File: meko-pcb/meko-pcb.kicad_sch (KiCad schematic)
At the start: 209 parts, among them IC2 TPS7A2033PDBVR, IC4 TAD5212IRGER, IC5 AS5600-ASOM, J1 USB_C_Receptacle_USB2.0_16P, J2 Conn_ARM_JTAG_SWD_10, J3 GDEY0154D67, J5 503398-1892, Q1 SS8050, Q2 Si1308EDL, SW1 SW_Push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

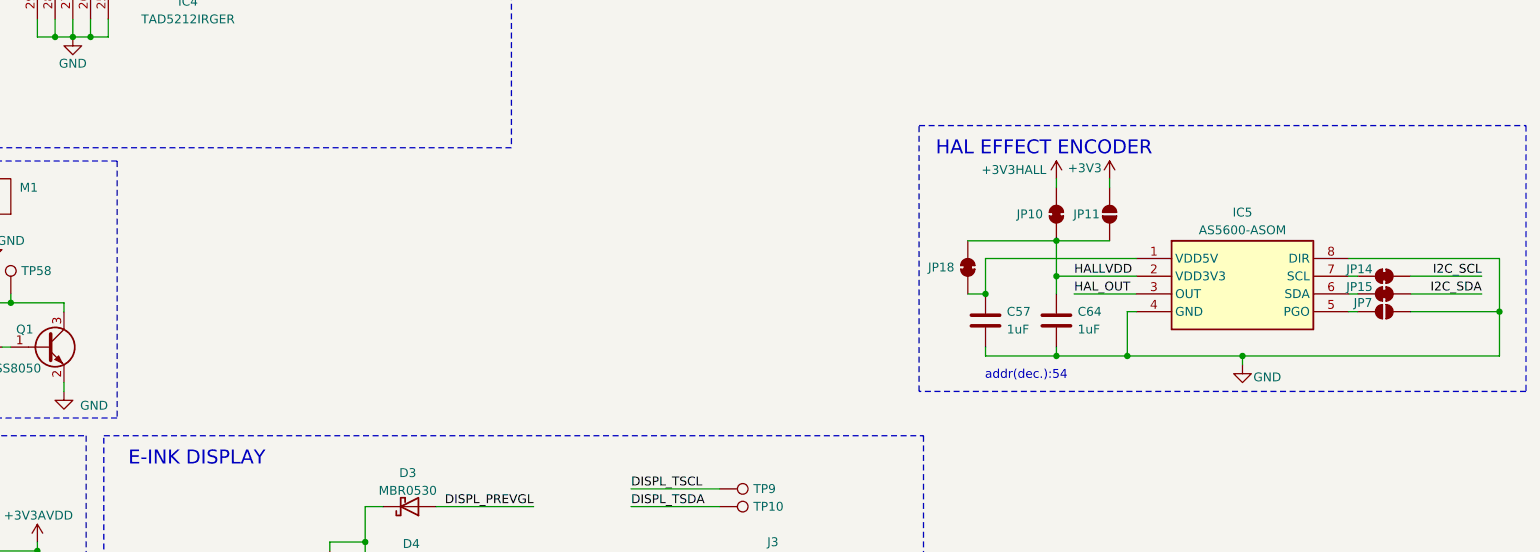
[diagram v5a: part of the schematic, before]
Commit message: updated a cap
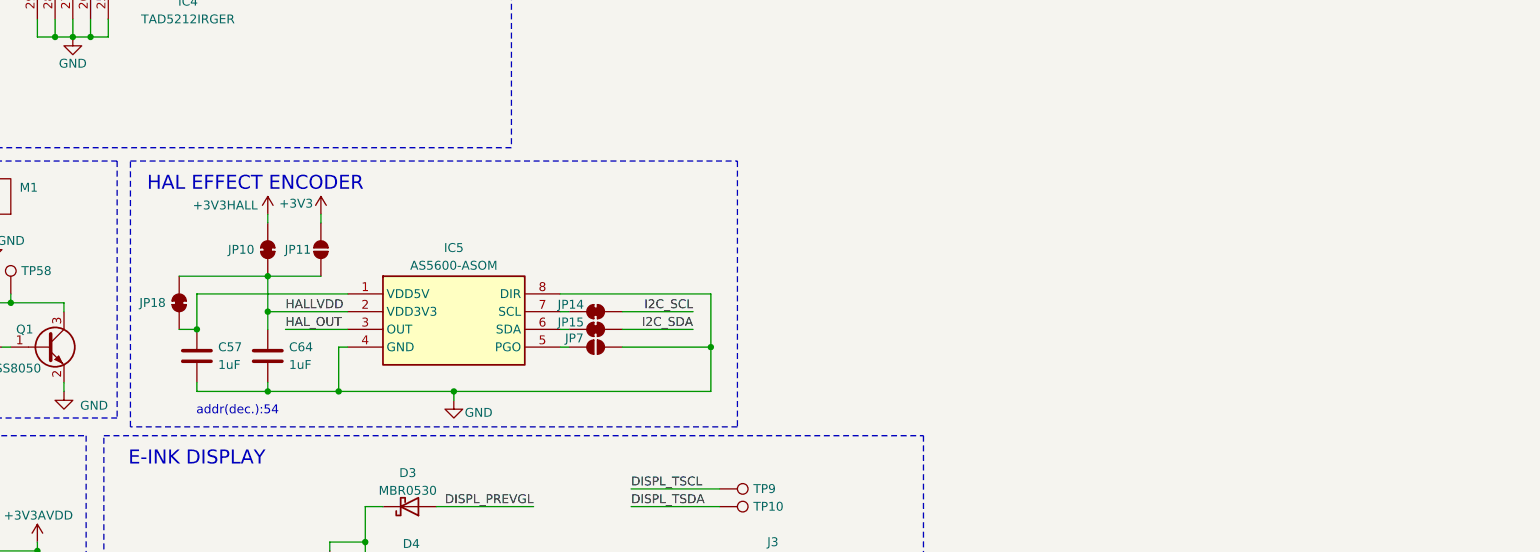
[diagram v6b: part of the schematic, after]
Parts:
- C18: LCSC C519367 -> C501844
- M1: LCSC (none) -> C2894731; LCSC Part Name LD-SM-430 -> (none); MPN LD-SM-430 -> (none); Manufacturer LEADER(立得) -> (none); Supplier LCSC -> (none); Supplier Part C41348533 -> (none)
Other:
- moved on the sheet: C57, C64, IC5, JP10, JP11, JP14, JP15, JP18, JP7

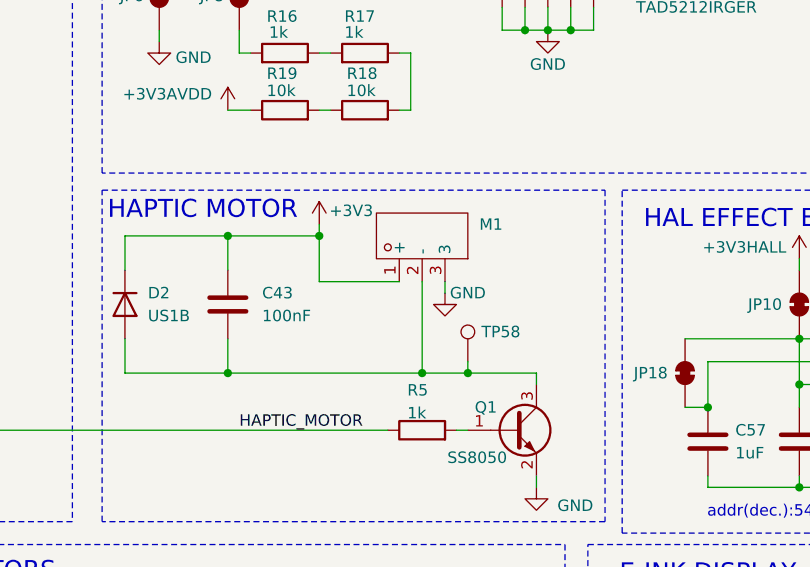
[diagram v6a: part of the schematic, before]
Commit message: updated motor foorprint, added 3d moedel
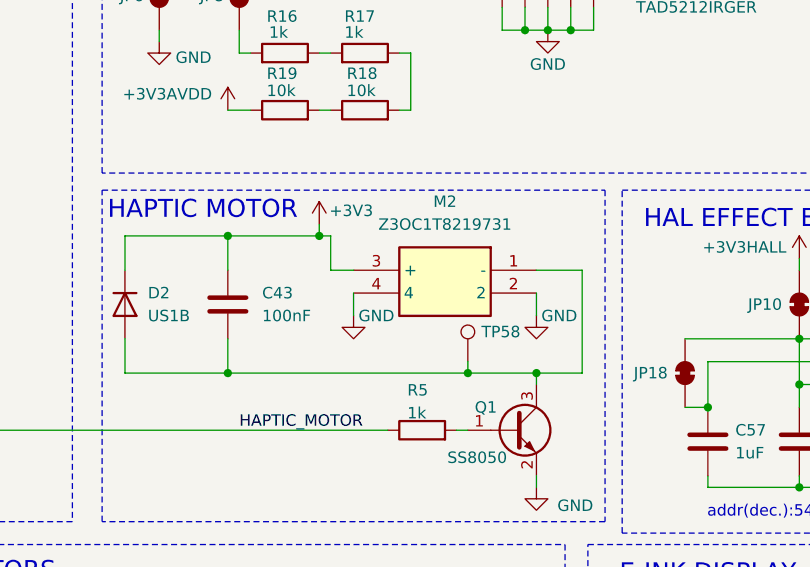
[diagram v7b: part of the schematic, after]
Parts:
- removed M1: ~, LD-SM-430:SMD_LD-SM-430-1, symbol LD-SM-430:LD-SM-430
- added M2: Z3OC1T8219731, Z3OC1T8219731:Z3OC1T8219731, symbol Z3OC1T8219731:Z3OC1T8219731
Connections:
- net +3V3: now also M2.3 (+)
- net GND: now also M2.2, M2.4
- net at C43.2, D2.2 (A), Q1.3 (C)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: now also M2.1 (-)

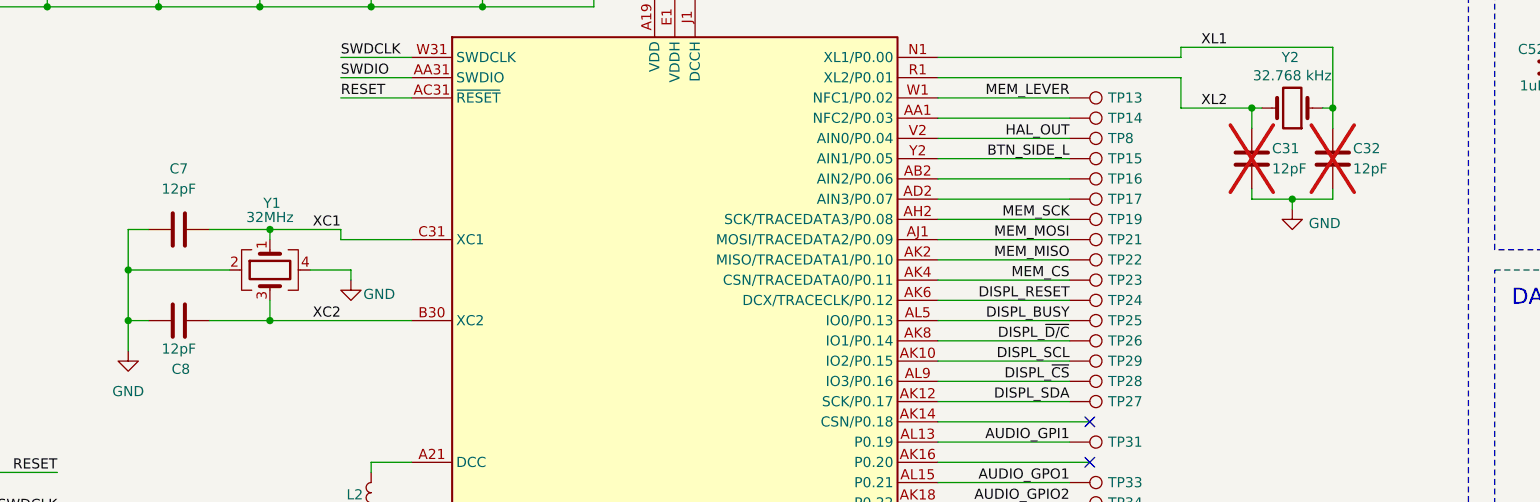
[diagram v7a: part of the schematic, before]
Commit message: chose a new crystal, so i can remove all 4 load caps
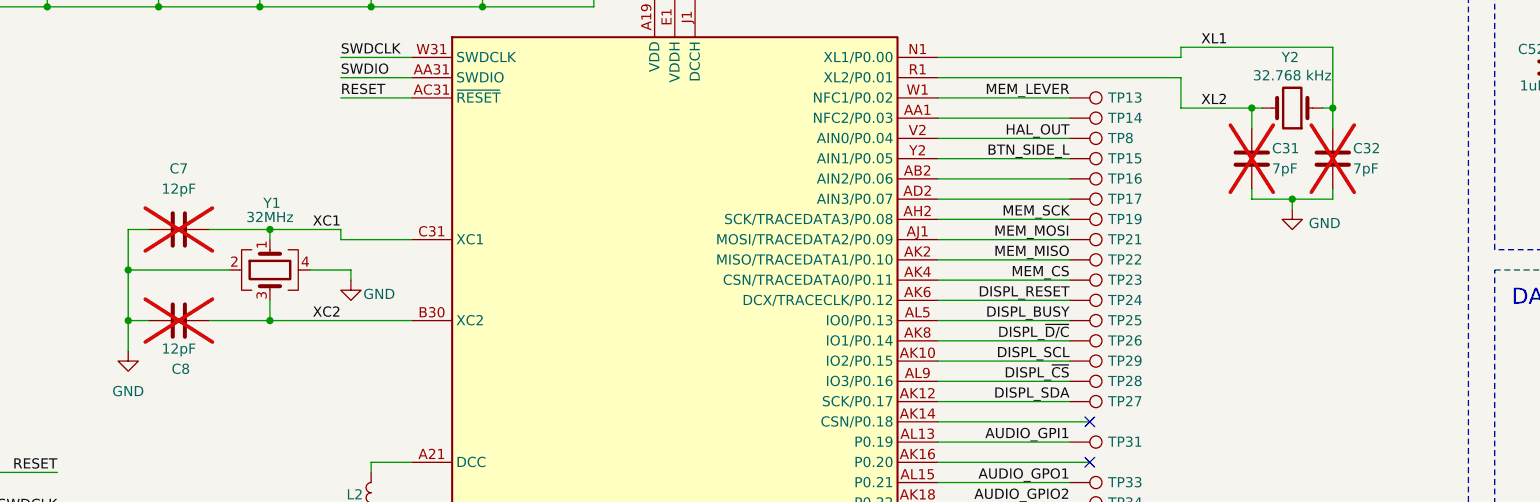
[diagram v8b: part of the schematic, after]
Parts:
- C31, C32: value 12pF -> 7pF; LCSC C38523 -> (none); MPN CL10C120JB8NNNC -> (none)
- C7, C8: now not fitted; now left out of the parts list
- Y2: LCSC C5213671 -> C90945
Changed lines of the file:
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@@
 			)
 		)
-		(property "Value" "12pF"
+		(property "Value" "7pF"
 			(at 228.6 116.84 0)
 			(effects
@@
 			)
 		)
-		(property "LCSC" "C38523"
+		(property "LCSC" ""
 			(at 226.06 115.57 0)
 			(effects
@@
 			)
 		)
-		(property "MPN" "CL10C120JB8NNNC"
+		(property "MPN" ""
 			(at 226.06 115.57 0)
 			(effects
@@
 			)
 		)
-		(property "Value" "12pF"
+		(property "Value" "7pF"
 			(at 218.44 116.84 0)
 			(effects
@@
 			)
 		)
-		(property "LCSC" "C38523"
+		(property "LCSC" ""
 			(at 215.9 115.57 0)
 			(effects
@@
 			)
 		)
-		(property "MPN" "CL10C120JB8NNNC"
+		(property "MPN" ""
 			(at 215.9 115.57 0)
 			(effects
@@
 		(unit 1)
 		(exclude_from_sim no)
-		(in_bom yes)
+		(in_bom no)
 		(on_board yes)
-		(dnp no)
+		(dnp yes)
 		(property "Reference" "C8"
 			(at 81.534 141.986 90)
@@
 		(unit 1)
 		(exclude_from_sim no)
-		(in_bom yes)
+		(in_bom no)
 		(on_board yes)
-		(dnp no)
+		(dnp yes)
 		(fields_autoplaced yes)
 		(property "Reference" "C7"
@@
 			)
 		)
-		(property "LCSC" "C5213671"
+		(property "LCSC" "C90945"
 			(at 220.98 109.22 0)
 			(effects
